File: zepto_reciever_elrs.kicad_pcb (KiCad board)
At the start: 4 copper layers, 12 x 9 mm, 50 parts, among them J1 u.fl, SW1 SW_Push, U1 STM32WLE5JBI6, U2 NCP160, U3 BGS12PL6E6327XTSA1, Y1 32MHz

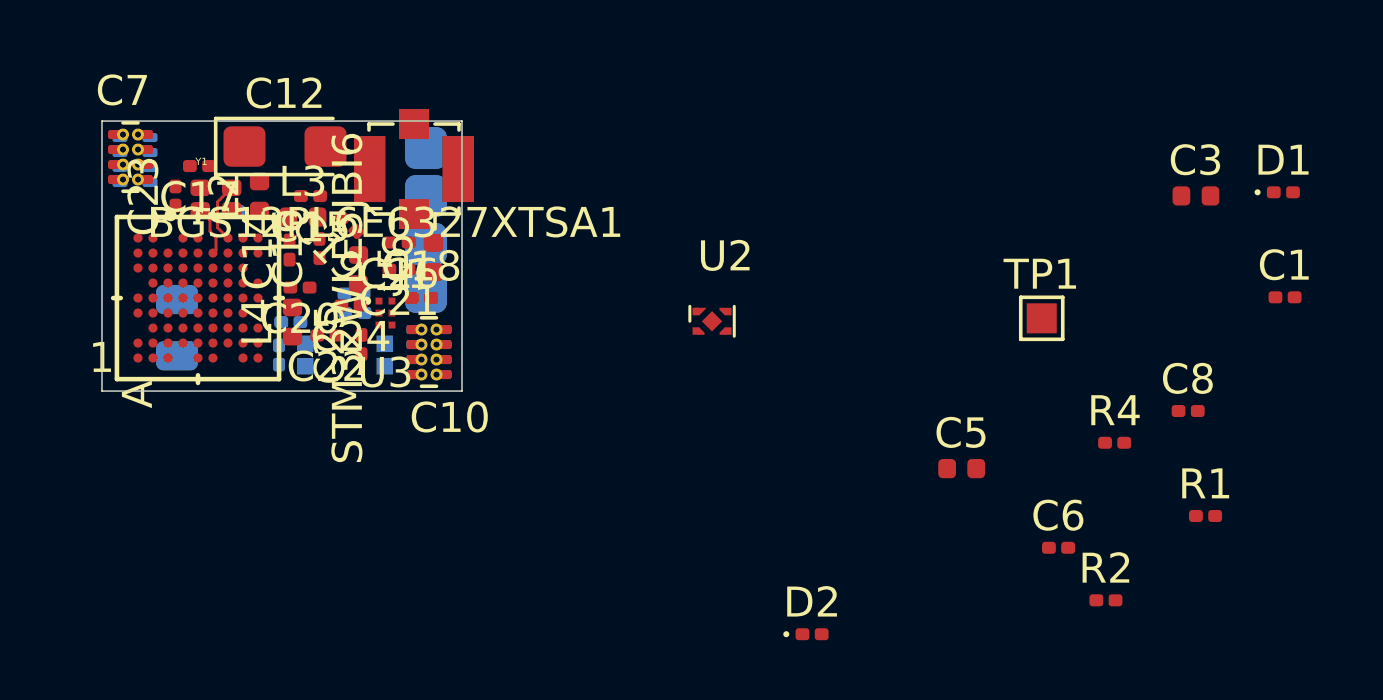
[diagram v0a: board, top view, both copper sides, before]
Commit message: Routed half of the Layout, changed a few pins
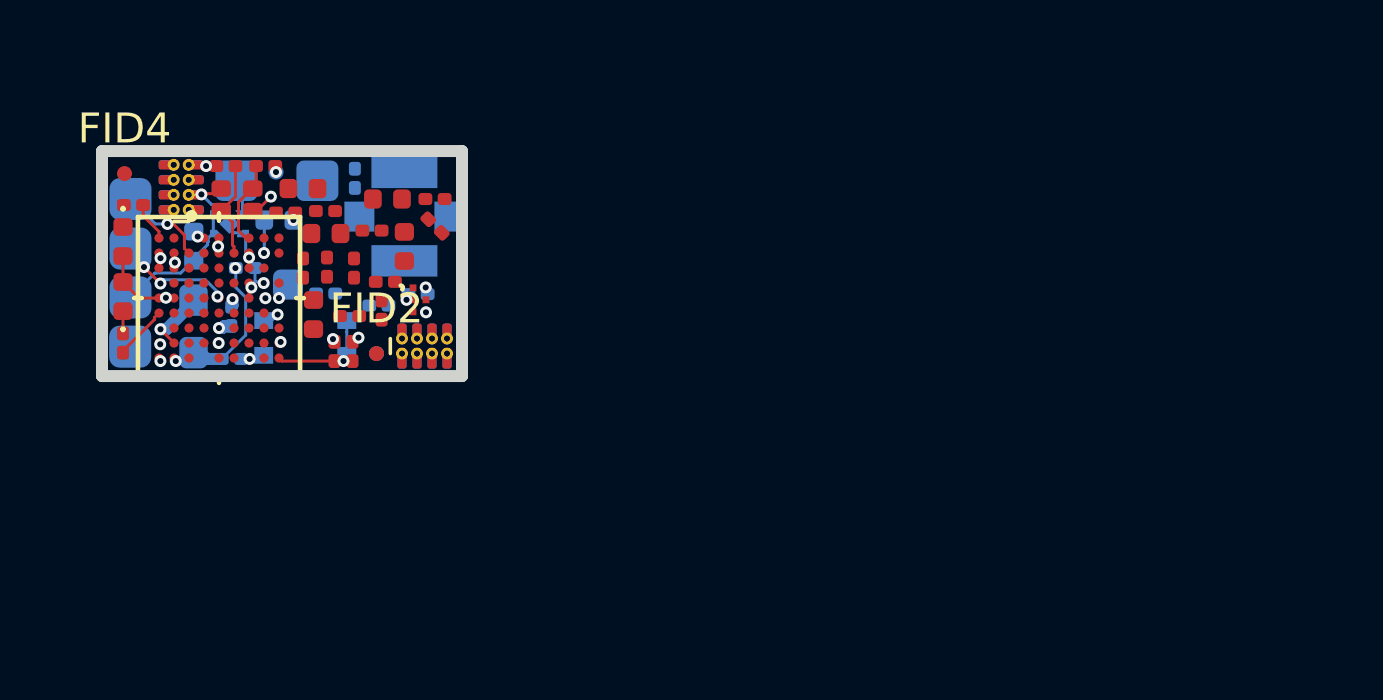
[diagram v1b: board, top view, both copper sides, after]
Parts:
- added FID1: Fiducial, Fiducial:Fiducial_0.5mm_Dia_1mm_Outer, B.Cu at (129.2, 57.8)
- added FID2: Fiducial, Fiducial:Fiducial_0.5mm_Dia_1mm_Outer, F.Cu at (129.2, 57.8)
- added FID3: Fiducial, Fiducial:Fiducial_0.5mm_Dia_1mm_Outer, B.Cu at (125.8, 51.7)
- added FID4: Fiducial, Fiducial:Fiducial_0.5mm_Dia_1mm_Outer, F.Cu at (120.8, 51.8)
- C1, C12, C26, C3, C5, C6, C8, J1, R4, TP1, U2: moved to B.Cu
- C2, C4, R3: moved to F.Cu
- D1, D2: footprint LED_SMD:LED_0201_0603Metric -> LED_SMD:LED_0402_1005Metric
- L1: footprint Inductor_SMD:L_0805_2012Metric -> Inductor_SMD:L_0603_1608Metric_Pad1.05x0.95mm_HandSolder
- R2: value 10k -> 270R
- SW1: footprint ftprnts:SW_EVP-BB2A9B000 -> ftprnts:EVPBL9A2B000
- moved D1 38.7 mm to (120.7, 54.0), turned to 270 degrees
- moved R1 37.2 mm to (121.0, 52.8), turned to 180 degrees
- moved C1 34.7 mm to (124.8, 54.9)
- moved R2 33.9 mm to (120.7, 57.4), turned to 90 degrees
- moved C3 33.4 mm to (123.1, 54.2), turned to 90 degrees
- moved C8 32.1 mm to (124.3, 56.5), turned to 270 degrees
- moved C6 28.3 mm to (124.3, 57.9)
- moved R4 26.8 mm to (127.5, 55.8), turned to 180 degrees
- moved D2 25.6 mm to (120.7, 55.9), turned to 90 degrees
- moved TP1 25.2 mm to (126.2, 55.5)
- moved C5 24.2 mm to (125.9, 53.3)
- moved U2 16.4 mm to (124.2, 53.4), turned to 180 degrees
- moved TP2 11.9 mm to (120.9, 57.5)
- moved TP3 9.85 mm to (121.0, 55.9)
- moved TP5 9.85 mm to (121.0, 54.2)
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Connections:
- U1 pad A4: Net-(U1-PadA4) -> LED2
- U1 pad A9: Net-(U1-PadA9) -> LED1
- U1 pad B8: Net-(U1-PadB8) -> GND
- U1 pad C1: LED1 -> Net-(U1-PadC1)
- U1 pad D7: BIND_BUT -> Net-(U1-PadD7)
- U1 pad E1: LED2 -> Net-(U1-PadE1)
- U1 pad F3: RFSW_CRTL -> Net-(U1-PadF3)
- U1 pad J1: Net-(U1-PadJ1) -> BIND_BUT
- U1 pad J2: Net-(U1-PadJ2) -> RFSW_CRTL
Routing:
- net GND: track 0.00 -> 10.6 mm, vias 0 -> 16
- net +3V3: track 0.00 -> 6.85 mm, vias 0 -> 9
- net VDDRF1V5: track 0.00 -> 5.43 mm, vias 0 -> 2
- net 3.3-5V_IN: track 0.00 -> 4.53 mm
- net Net-(L1-Pad1): track 0.00 -> 3.74 mm, vias 0 -> 1
- net BIND_BUT: track 0.00 -> 3.29 mm, vias 0 -> 1
- net UART_TX: track 0.00 -> 3.12 mm, vias 0 -> 3
- net UART_RX: track 0.00 -> 2.96 mm, vias 0 -> 1
- net LED2: track 0.00 -> 1.82 mm
- net XO: track 1.68 -> 3.34 mm
- net LED1: track 0.00 -> 1.32 mm
- net XI: track 2.02 -> 2.95 mm
- net Net-(D2-Pad1): track 0.00 -> 0.74 mm
- net Net-(C8-Pad1): track 0.00 -> 0.35 mm, vias 0 -> 1
- net RFSW_CRTL: track 0.00 -> 0.07 mm, vias 0 -> 1
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- added copper zone on In2.Cu, net +3V3
- added copper zone on In1.Cu, net GND
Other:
- board size 12 x 9 mm -> 12 x 7.5 mm
